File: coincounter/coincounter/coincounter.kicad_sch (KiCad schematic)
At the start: 33 parts, among them J1 Conn_01x03, SW1 SW_Coded_SH-7010, SW2 SW_Coded_SH-7010, U1 93LC46A, U2 UPD75P0076, Y1 Crystal

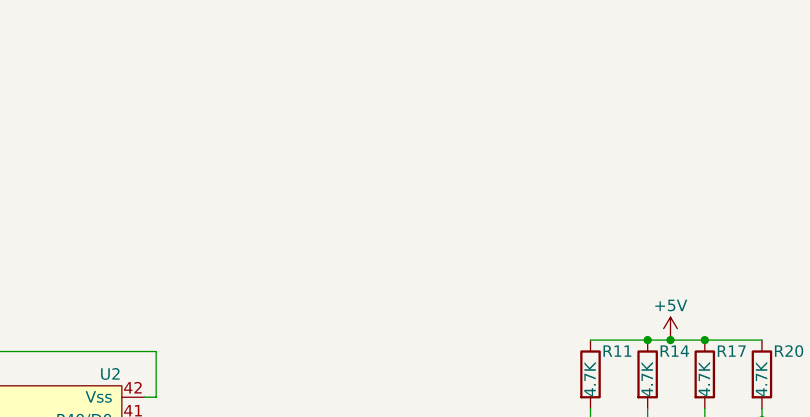
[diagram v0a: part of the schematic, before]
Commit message: Add flashing tool schematic, reorganize arduino files so the ide doesn't get confused, and improve ledstripesplitter so it even retimes the high pulses if the input is out of whack.
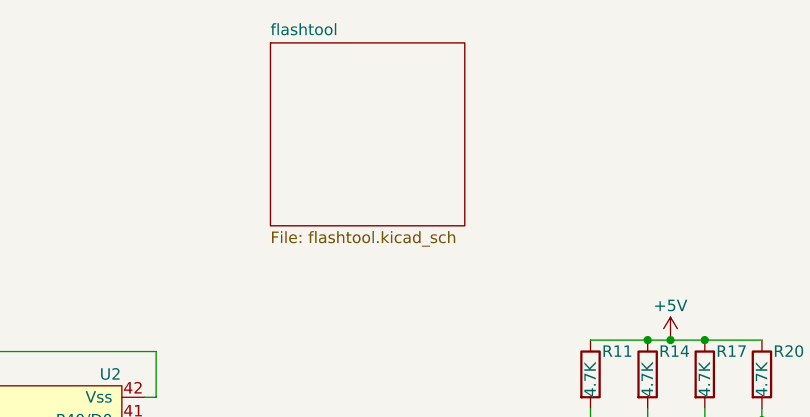
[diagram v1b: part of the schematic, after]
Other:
- added sheet flashtool (flashtool.kicad_sch)
